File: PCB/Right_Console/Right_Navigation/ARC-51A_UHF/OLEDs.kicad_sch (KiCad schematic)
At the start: 10 parts, among them U4 TCA9548APWR, U5 FREQ_LOW_OLED, U6 UHF_PRE_OLED, U7 FREQ_HI_OLED

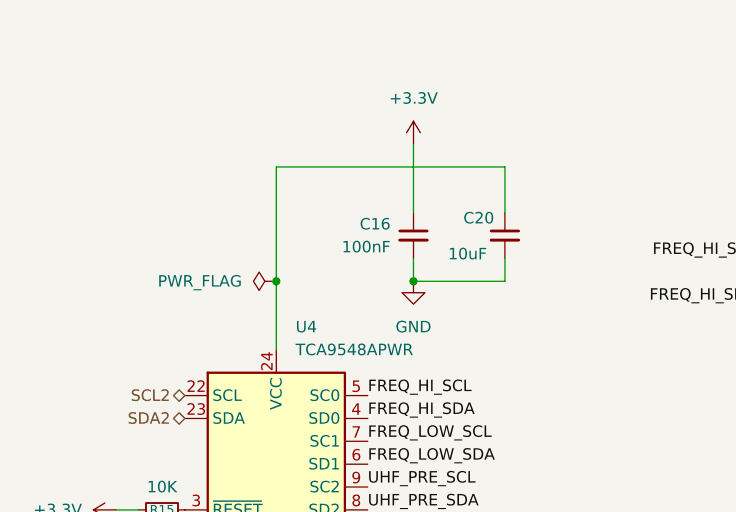
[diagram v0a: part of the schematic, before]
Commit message: fix(pcb): ARC-51A_UHF — drop disconnected +3V3 stub + stray PWR_FLAGs on OLED sheet
Removed two orphaned PWR_FLAG symbols and the disconnected +3V3 wire island
they sat on (OLEDs sheet). Real +3V3 net stays driven from the connector
sheet; ERC clean (0 violations). No components affected.
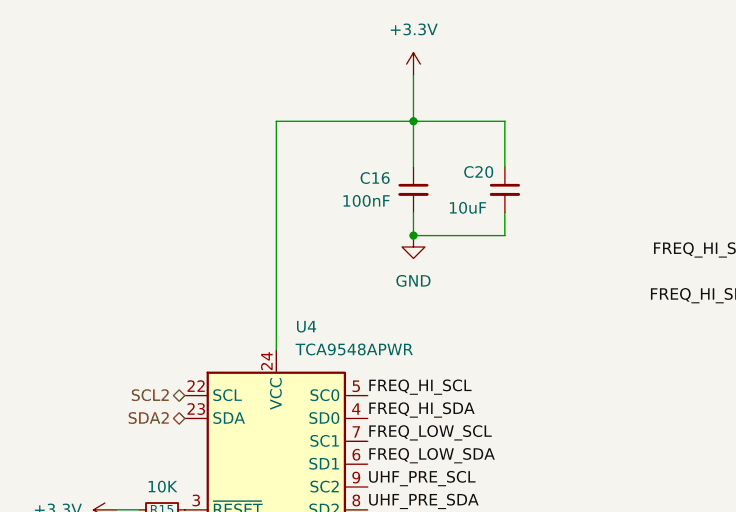
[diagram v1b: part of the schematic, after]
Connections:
- net +3.3V: now also C20.1, U4.24 (VCC)
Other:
- moved on the sheet: C16, C20
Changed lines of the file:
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@@
 	(paper "A4")
 	(junction
-		(at 81.28 58.42)
+		(at 81.28 40.64)
+		(diameter 0)
+		(color 0 0 0 0)
+	)
+	(junction
+		(at 81.28 53.34)
 		(diameter 0)
 		(color 0 0 0 0)
@@
 	)
 	(junction
-		(at 66.04 58.42)
-		(diameter 0)
-		(color 0 0 0 0)
-	)
-	(junction
 		(at 134.62 142.24)
 		(diameter 0)
@@
 	(wire
 		(pts
+			(xy 81.28 40.64) (xy 91.44 40.64)
+		)
+		(stroke
+			(width 0)
+			(type default)
+		)
+	)
+	(wire
+		(pts
 			(xy 119.38 111.76) (xy 124.46 111.76)
 		)
@@
 	(wire
 		(pts
-			(xy 81.28 58.42) (xy 91.44 58.42)
+			(xy 81.28 53.34) (xy 91.44 53.34)
 		)
 		(stroke
@@
 	(wire
 		(pts
+			(xy 81.28 35.56) (xy 81.28 40.64)
+		)
+		(stroke
+			(width 0)
+			(type default)
+		)
+	)
+	(wire
+		(pts
 			(xy 134.62 40.64) (xy 147.32 40.64)
 		)
@@
 	(wire
 		(pts
-			(xy 66.04 45.72) (xy 66.04 58.42)
-		)
-		(stroke
-			(width 0)
-			(type default)
-		)
-	)
-	(wire
-		(pts
-			(xy 81.28 58.42) (xy 81.28 55.88)
-		)
-		(stroke
-			(width 0)
-			(type default)
-		)
-	)
-	(wire
-		(pts
-			(xy 81.28 43.18) (xy 81.28 50.8)
+			(xy 81.28 53.34) (xy 81.28 50.8)
 		)
 		(stroke
@@
 	(wire
 		(pts
-			(xy 66.04 45.72) (xy 91.44 45.72)
+			(xy 66.04 40.64) (xy 81.28 40.64)
 		)
 		(stroke
@@
 	(wire
 		(pts
-			(xy 66.04 58.42) (xy 66.04 66.04)
+			(xy 66.04 40.64) (xy 66.04 66.04)
+		)
+		(stroke
+			(width 0)
+			(type default)
+		)
+	)
+	(wire
+		(pts
+			(xy 81.28 40.64) (xy 81.28 45.72)
 		)
 		(stroke
@@
 	(wire
 		(pts
-			(xy 91.44 58.42) (xy 91.44 55.88)
+			(xy 91.44 53.34) (xy 91.44 50.8)
 		)
 		(stroke
@@
 	(wire
 		(pts
-			(xy 91.44 45.72) (xy 91.44 50.8)
+			(xy 91.44 40.64) (xy 91.44 45.72)
 		)
 		(stroke
@@
 	(symbol
 		(lib_id "power:GND")
-		(at 81.28 58.42 0)
+		(at 81.28 53.34 0)
 		(unit 1)
 		(body_style 1)
@@
 		(fields_autoplaced yes)
 		(property "Reference" "#PWR043"
-			(at 81.28 64.77 0)
+			(at 81.28 59.69 0)
 			(hide yes)
 			(show_name no)
@@
 		)
 		(property "Value" "GND"
-			(at 81.28 63.5 0)
+			(at 81.28 58.42 0)
 			(show_name no)
 			(do_not_autoplace no)
@@
 		)
 		(property "Footprint" ""
-			(at 81.28 58.42 0)
+			(at 81.28 53.34 0)
 			(hide yes)
 			(show_name no)
@@
 		)
 		(property "Datasheet" ""
-			(at 81.28 58.42 0)
+			(at 81.28 53.34 0)
 			(hide yes)
 			(show_name no)
@@
 		)
 		(property "Description" "Power symbol creates a global label with name \"GND\" , ground"
-			(at 81.28 58.42 0)
+			(at 81.28 53.34 0)
 			(hide yes)
 			(show_name no)
@@
 	(symbol
 		(lib_id "power:+3.3V")
-		(at 81.28 43.18 0)
+		(at 81.28 35.56 0)
 		(unit 1)
 		(body_style 1)
@@
 		(fields_autoplaced yes)
 		(property "Reference" "#PWR042"
-			(at 81.28 46.99 0)
+			(at 81.28 39.37 0)
 			(hide yes)
 			(show_name no)
@@
 		)
 		(property "Value" "+3.3V"
-			(at 81.28 38.1 0)
+			(at 81.28 30.48 0)
 			(show_name no)
 			(do_not_autoplace no)
@@
 		)
 		(property "Footprint" ""
-			(at 81.28 43.18 0)
+			(at 81.28 35.56 0)
 			(hide yes)
 			(show_name no)
@@
 		)
 		(property "Datasheet" ""
-			(at 81.28 43.18 0)
+			(at 81.28 35.56 0)
 			(hide yes)
 			(show_name no)
@@
 		)
 		(property "Description" "Power symbol creates a global label with name \"+3.3V\""
-			(at 81.28 43.18 0)
+			(at 81.28 35.56 0)
 			(hide yes)
 			(show_name no)
@@
 	(symbol
 		(lib_id "Device:C_Small")
-		(at 91.44 53.34 0)
+		(at 91.44 48.26 0)
 		(unit 1)
 		(body_style 1)
@@
 		(dnp no)
 		(property "Reference" "C20"
-			(at 86.8222 51.405 0)
+			(at 86.8222 46.325 0)
 			(show_name no)
 			(do_not_autoplace no)
@@
 		)
 		(property "Value" "10uF"
-			(at 85.1297 55.3873 0)
+			(at 85.1297 50.3073 0)
 			(show_name no)
 			(do_not_autoplace no)
@@
 		)
 		(property "Footprint" "Capacitor_SMD:C_0805_2012Metric"
-			(at 91.44 53.34 0)
+			(at 91.44 48.26 0)
 			(hide yes)
 			(show_name no)
@@
 		)
 		(property "Datasheet" ""
-			(at 91.44 53.34 0)
+			(at 91.44 48.26 0)
 			(hide yes)
 			(show_name no)
@@
 		)
 		(property "Description" "Unpolarized capacitor, small symbol"
-			(at 91.44 53.34 0)
+			(at 91.44 48.26 0)
 			(hide yes)
 			(show_name no)
@@
 		)
 		(property "LCSC" ""
-			(at 17.78 13.97 0)
+			(at 17.78 8.89 0)
 			(hide yes)
 			(show_name no)
@@
 		)
 		(property "Tolerance" "20%"
-			(at 17.78 13.97 0)
+			(at 17.78 8.89 0)
 			(hide yes)
 			(show_name no)
@@
 		)
 		(property "Rating" "25V"
-			(at 17.78 13.97 0)
+			(at 17.78 8.89 0)
 			(hide yes)
 			(show_name no)
@@
 		)
 		(property "Notes" ""
-			(at 17.78 13.97 0)
+			(at 17.78 8.89 0)
 			(hide yes)
 			(show_name no)
@@
 				(path "/36bf5781-4cca-401f-9481-4fe5a5518389/963b41a2-2e68-4e24-89d4-9bad601c39fc"
 					(reference "#PWR048")
-					(unit 1)
-				)
-			)
-		)
-	)
-	(symbol
-		(lib_id "power:PWR_FLAG")
-		(at 66.04 58.42 90)
-		(unit 1)
-		(body_style 1)
-		(exclude_from_sim no)
-		(in_bom yes)
-		(on_board yes)
-		(in_pos_files yes)
-		(dnp no)
-		(fields_autoplaced yes)
-		(property "Reference" "#FLG01"
-			(at 64.135 58.42 0)
-			(hide yes)
-			(show_name no)
-			(do_not_autoplace no)
-			(effects
-				(font
-					(size 1.27 1.27)
-				)
-			)
-		)
-		(property "Value" "PWR_FLAG"
-			(at 62.23 58.4199 90)
-			(show_name no)
-			(do_not_autoplace no)
-			(effects
-				(font
-					(size 1.27 1.27)
-				)
-				(justify left)
-			)
-		)
-		(property "Footprint" ""
-			(at 66.04 58.42 0)
-			(hide yes)
-			(show_name no)
-			(do_not_autoplace no)
-			(effects
-				(font
-					(size 1.27 1.27)
-				)
-			)
-		)
-		(property "Datasheet" ""
-			(at 66.04 58.42 0)
-			(hide yes)
-			(show_name no)
-			(do_not_autoplace no)
-			(effects
-				(font
-					(size 1.27 1.27)
-				)
-			)
-		)
-		(property "Description" "Special symbol for telling ERC where power comes from"
-			(at 66.04 58.42 0)
-			(hide yes)
-			(show_name no)
-			(do_not_autoplace no)
-			(effects
-				(font
-					(size 1.27 1.27)
-				)
-			)
-		)
-		(pin "1"
-		)
-		(instances
-			(project "ARC-51A_UHF"
-				(path "/36bf5781-4cca-401f-9481-4fe5a5518389/963b41a2-2e68-4e24-89d4-9bad601c39fc"
-					(reference "#FLG01")
 					(unit 1)
 				)
@@
 	(symbol
 		(lib_id "Device:C_Small")
-		(at 81.28 53.34 0)
+		(at 81.28 48.26 0)
 		(unit 1)
 		(body_style 1)
@@
 		(fields_autoplaced yes)
 		(property "Reference" "C16"
-			(at 78.74 52.0762 0)
+			(at 78.74 46.9962 0)
 			(show_name no)
 			(do_not_autoplace no)
@@
 		)
 		(property "Value" "100nF"
-			(at 78.74 54.6162 0)
+			(at 78.74 49.5362 0)
 			(show_name no)
 			(do_not_autoplace no)
@@
 		)
 		(property "Footprint" "Capacitor_SMD:C_0805_2012Metric"
-			(at 81.28 53.34 0)
+			(at 81.28 48.26 0)
 			(hide yes)
 			(show_name no)
@@
 		)
 		(property "Datasheet" ""
-			(at 81.28 53.34 0)
+			(at 81.28 48.26 0)
 			(hide yes)
 			(show_name no)
@@
 		)
 		(property "Description" "Unpolarized capacitor, small symbol"
-			(at 81.28 53.34 0)
+			(at 81.28 48.26 0)
 			(hide yes)
 			(show_name no)
@@
 		)
 		(property "LCSC" ""
-			(at 7.62 13.97 0)
+			(at 7.62 8.89 0)
 			(hide yes)
 			(show_name no)
@@
 		)
 		(property "Tolerance" "10%"
-			(at 7.62 13.97 0)
+			(at 7.62 8.89 0)
 			(hide yes)
 			(show_name no)
@@
 		)
 		(property "Rating" "50V"
-			(at 7.62 13.97 0)
+			(at 7.62 8.89 0)
 			(hide yes)
 			(show_name no)
@@
 		)
 		(property "Notes" ""
-			(at 7.62 13.97 0)
-			(hide yes)
-			(show_name no)
+			(at 7.62 8.89 0)
+			(hide yes)
+			(show_name no)

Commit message: feat(pcb): label LCSC/tolerance/voltage on Right_Nav + PDU schematics
Populate LCSC, Tolerance, and Rating (voltage/power) fields across the four
fabbed boards, sourced from InvenTree + the board tickets and PDU DESIGN-NOTES.
Values corrected to the selected part (100nF 50V, resistors 1%, AMS1117
C6186 -> C347222, 10uF split 25V/35V by +12V rail).

- PDU: dividers 0.1% (C2828767/C865184/C406725/C110774), J1 Mini-Fit 4-pin
  C20608114, D3/D4 green, C9 35V on +12V (SMBJ12A clamp margin).
- ARC-51A: MCP23017 C506653, TCA9548 C130026, J9 XH-8 C23067548, backlight
  J8 Mini-Fit 2-pin C20608113.
- ASN-41: AMS1117 C347222, TCA9548 C130026, 10uF per-rail split, 74HC165 x4
  C22384789, 1k ADC filter C844939, backlight J8 C20608113.
- APN-153: footprints (0805 passives + XH/Mini-Fit connectors) + MCP23017
  C506653, DRV8833 C50506, 2N7002 C8545, 2.2uF C87994 (25V X5R), 10nF C1710,
  6-pin XH J2 C23067546.

Off-board panel controls (encoders, rotary switches, OLED, pot, stepper, MEM
button) excluded as connector-coupled. Pin headers (SWD, CAN_TERM) hand-
soldered, no assembly LCSC. Harness mating ends tracked in the order BOM.
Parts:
- C16, C17, C18, C19: LCSC (none) -> C1711
- C20: LCSC (none) -> C669099
- R15: LCSC (none) -> C844937
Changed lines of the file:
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@@
 			)
 		)
-		(property "LCSC" ""
+		(property "LCSC" "C1711"
 			(at 15.24 2.54 0)
 			(hide yes)
@@
 			)
 		)
-		(property "LCSC" ""
+		(property "LCSC" "C669099"
 			(at 17.78 8.89 0)
 			(hide yes)
@@
 			)
 		)
-		(property "LCSC" ""
+		(property "LCSC" "C1711"
 			(at 16.51 50.8 0)
 			(hide yes)
@@
 			)
 		)
-		(property "LCSC" ""
+		(property "LCSC" "C1711"
 			(at 16.51 -54.61 0)
 			(hide yes)
@@
 			)
 		)
-		(property "LCSC" ""
+		(property "LCSC" "C844937"
 			(at 17.78 22.86 0)
 			(hide yes)
@@
 			)
 		)
-		(property "LCSC" ""
+		(property "LCSC" "C1711"
 			(at 7.62 8.89 0)
 			(hide yes)

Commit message: chore(pcb): normalize passive value-string case fleet-wide
Cosmetic cleanup — standardize resistor/cap value strings so identical
parts stop showing as separate BOM lines. Value = magnitude only;
tolerance + LCSC carry the precision distinction.

- 10K -> 10k, 4.7K -> 4.7k, 100K -> 100k (lowercase SI k)
- 100nf -> 100nF
- 69 symbols across all 6 boards (ASN-41, ARC-51A, APN-153, PDU,
  Gateway_Bridge, PanelGroup_Base). ERC 0/0 on all.

No functional/footprint/LCSC change. PDU generic 10k and precision
divider 10k now both read "10k", distinguished by tolerance (1% vs 0.1%).
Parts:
- R15: value 10K -> 10k
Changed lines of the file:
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@@
 			)
 		)
-		(property "Value" "10K"
+		(property "Value" "10k"
 			(at 53.34 81.28 90)
 			(show_name no)

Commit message: refactor(pcb): consolidate ceramic 10uF to single 35V part
The 10uF ceramic 0805 caps were split across two SKUs — C669099 (25V)
and C49010152 (35V) — distinguished only by rail. Standardize all 8
ceramic positions to the 35V part (C49010152); 35V covers the 25V
positions and collapses the BOM to one ceramic 10uF value.

Electrolytic 10uF (C3343) unchanged. Aluminum-bulk replacement deferred
to a future round. 8 caps across all 6 boards, ERC 0/0.
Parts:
- C20: LCSC C669099 -> C49010152; Rating 25V -> 35V
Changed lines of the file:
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@@
 			)
 		)
-		(property "LCSC" "C669099"
+		(property "LCSC" "C49010152"
 			(at 17.78 8.89 0)
 			(hide yes)
@@
 			)
 		)
-		(property "Rating" "25V"
+		(property "Rating" "35V"
 			(at 17.78 8.89 0)
 			(hide yes)

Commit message: fix(pcb): right-size MCP23017/TCA9548 bulk 10uF->1uF (ARC/APN)
The 10uF ceramic bulk beside the MCP23017 and TCA9548 (ARC C2/C20,
APN C2) is oversized: both are low-current I2C parts whose datasheets
call for only 0.1uF, already present. Drop to 1uF (reuse C28323, 0805
unchanged) — keeps ample bulk, frees the 10uF/35V ceramic. No footprint
or symbol change; ERC clean.
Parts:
- C20: value 10uF -> 1uF; LCSC C49010152 -> C28323; Rating 35V -> 50V; Tolerance 20% -> 10%
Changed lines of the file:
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@@
 			)
 		)
-		(property "Value" "10uF"
+		(property "Value" "1uF"
 			(at 85.1297 50.3073 0)
 			(show_name no)
@@
 			)
 		)
-		(property "LCSC" "C49010152"
+		(property "LCSC" "C28323"
 			(at 17.78 8.89 0)
 			(hide yes)
@@
 			)
 		)
-		(property "Tolerance" "20%"
+		(property "Tolerance" "10%"
 			(at 17.78 8.89 0)
 			(hide yes)
@@
 			)
 		)
-		(property "Rating" "35V"
+		(property "Rating" "50V"
 			(at 17.78 8.89 0)
 			(hide yes)

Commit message: feat(pcb): add descriptive IPN field to all on-board symbols (#238 Phase 3) (#239)
Phase 3 of the IPN convention (#238): adds a stable, descriptive
**Internal Part Number** to every on-board symbol, co-equal with LCSC.
BOMs now anchor on a fixed identity; the LCSC can change with
availability without altering the part's identity.

## What changed
- **352 symbols** across all 6 boards (multi-sheet aware) get an `IPN`
field. **51 distinct IPNs.** ERC clean fleet-wide.
- **Off-board controls** (encoders/switches/pots/OLED/stepper — no
footprint, connector-coupled) get **no IPN**, per the standing off-board
exclusion. On-board modules (RP2040-ZERO) and the RESET tact switch
**do** get IPNs.
- `.gitignore`: FreeCAD backups (`*.FCBak`/`*.FCStd1`) + KiCad ERC/DRC
reports (`*-erc.rpt`/`*-drc.rpt`).

## Scheme (descriptive, locked in #238)
`RES-10K-1PCT-0805` · `CAP-CER-100NF-50V-0805` · `CAP-ELEC-22UF-16V-D4`
· `IC-STM32F103C8-LQFP` · `CONN-XH-8P` · `TVS-SMBJ12A-SMB` ·
`FUSE-HOLDER-BLADE-DIP4` · `SW-TACT-6MM` · `MOD-RP2040-ZERO`.

Resolved the 3 open encoding items: ferrite → `FB-600R-0805` (TDK
600Ω@100MHz), NTC → `NTC-10K-1206` (APV 10K), fuse holder (C19727305 is
a *holder*, not a fuse) → one `FUSE-HOLDER-BLADE-DIP4`.

## Not in this PR (later phases of #238)
- **Phase 2 — InvenTree:** set the IPN field + link SupplierParts incl
backorder alternates (one IPN → many LCSC). This is what actually
delivers the churn-proofing; needs reviewed InvenTree writes.
- **Phase 4 — order flow:** resolve IPN → in-stock LCSC at order time.

Refs #238.
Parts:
- C16, C17, C18, C19: IPN (none) -> CAP-CER-100NF-50V-0805
- C20: IPN (none) -> CAP-CER-1UF-50V-0805
- R15: IPN (none) -> RES-10K-1PCT-0805
- U4: IPN (none) -> IC-TCA9548A-SSOP
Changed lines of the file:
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@@
+			)
+		)
+		(property "IPN" "CAP-CER-100NF-50V-0805"
+			(at 147.32 43.18 0)
+			(hide yes)
+			(show_name no)
+			(do_not_autoplace no)
+			(effects
+				(font
+					(size 1.27 1.27)
+				)
 			)
 		)
@@
 			)
 		)
+		(property "IPN" "CAP-CER-1UF-50V-0805"
+			(at 91.44 48.26 0)
+			(hide yes)
+			(show_name no)
+			(do_not_autoplace no)
+			(effects
+				(font
+					(size 1.27 1.27)
+				)
+			)
+		)
 		(property "Description" "Unpolarized capacitor, small symbol"
 			(at 91.44 48.26 0)
@@
 		)
 		(property "Datasheet" ""
+			(at 147.32 144.78 0)
+			(hide yes)
+			(show_name no)
+			(do_not_autoplace no)
+			(effects
+				(font
+					(size 1.27 1.27)
+				)
+			)
+		)
+		(property "IPN" "CAP-CER-100NF-50V-0805"
 			(at 147.32 144.78 0)
 			(hide yes)
@@
 			)
 		)
+		(property "IPN" "CAP-CER-100NF-50V-0805"
+			(at 147.32 93.98 0)
+			(hide yes)
+			(show_name no)
+			(do_not_autoplace no)
+			(effects
+				(font
+					(size 1.27 1.27)
+				)
+			)
+		)
 		(property "Description" "Unpolarized capacitor, small symbol"
 			(at 147.32 93.98 0)
@@
 		)
 		(property "Datasheet" ""
+			(at 53.34 83.82 0)
+			(hide yes)
+			(show_name no)
+			(do_not_autoplace no)
+			(effects
+				(font
+					(size 1.27 1.27)
+				)
+			)
+		)
+		(property "IPN" "RES-10K-1PCT-0805"
 			(at 53.34 83.82 0)
 			(hide yes)
@@
 			)
 		)
+		(property "IPN" "IC-TCA9548A-SSOP"
+			(at 67.31 82.55 0)
+			(hide yes)
+			(show_name no)
+			(do_not_autoplace no)
+			(effects
+				(font
+					(size 1.27 1.27)
+				)
+			)
+		)
 		(property "Description" "Low voltage 8-channel I2C switch with reset, TSSOP-24"
 			(at 66.04 88.9 0)
@@
 			(at 81.28 48.26 0)
 			(hide yes)
+			(show_name no)
+			(do_not_autoplace no)
+			(effects
+				(font
+					(size 1.27 1.27)
+				)
+			)
+		)
+		(property "IPN" "CAP-CER-100NF-50V-0805"
+			(at 81.28 48.26 0)
+			(hide yes)
